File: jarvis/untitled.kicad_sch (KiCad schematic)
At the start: 17 parts, among them IC3 MCP73871T-4CAI_ML, IC4 TLV70033DDCT, J3 Conn_01x02 - Battery, U2 2137160001

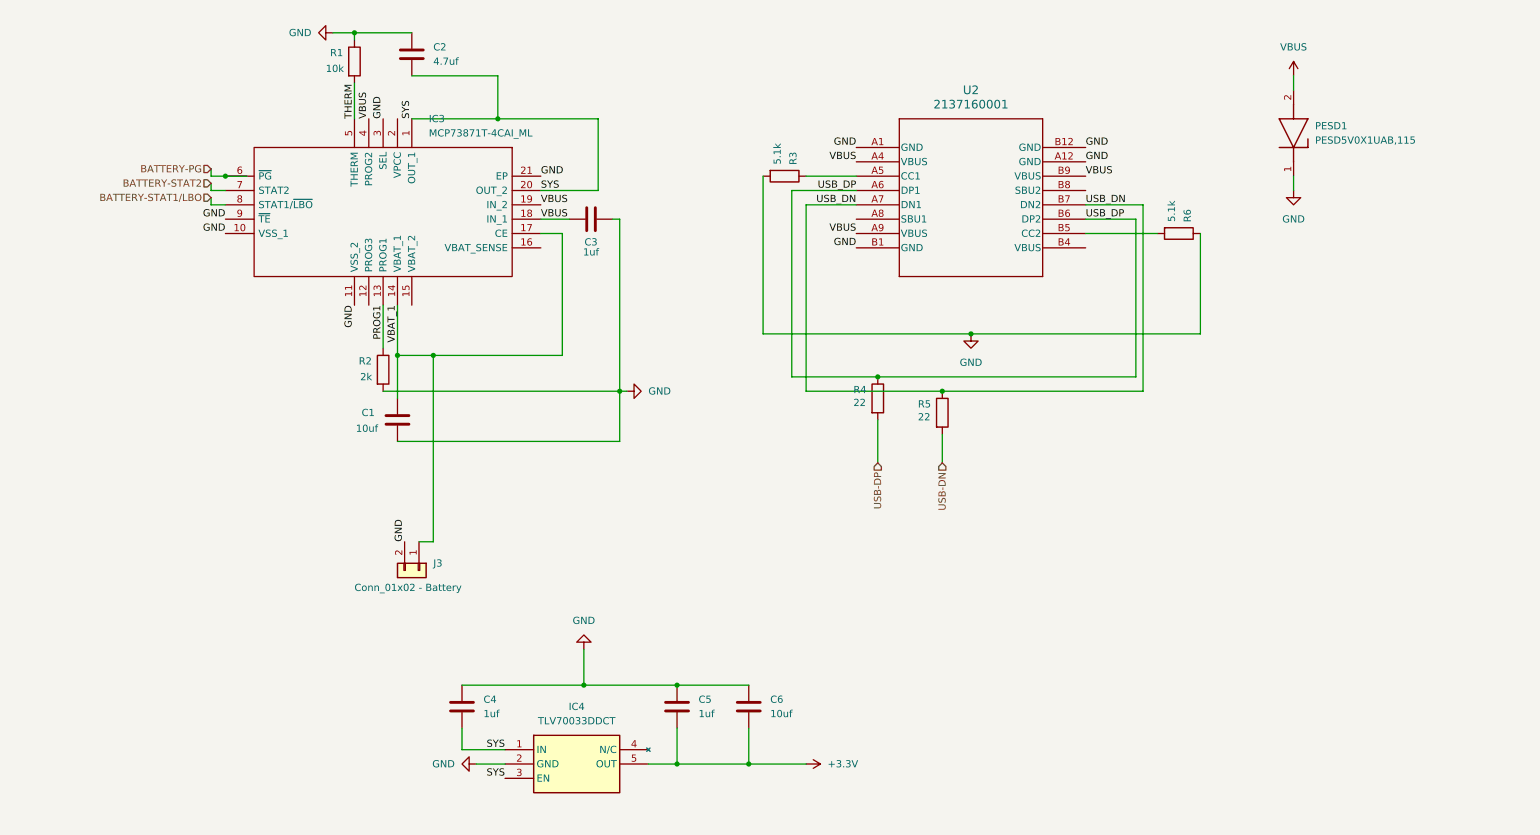
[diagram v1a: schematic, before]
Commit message: with leds and boot button
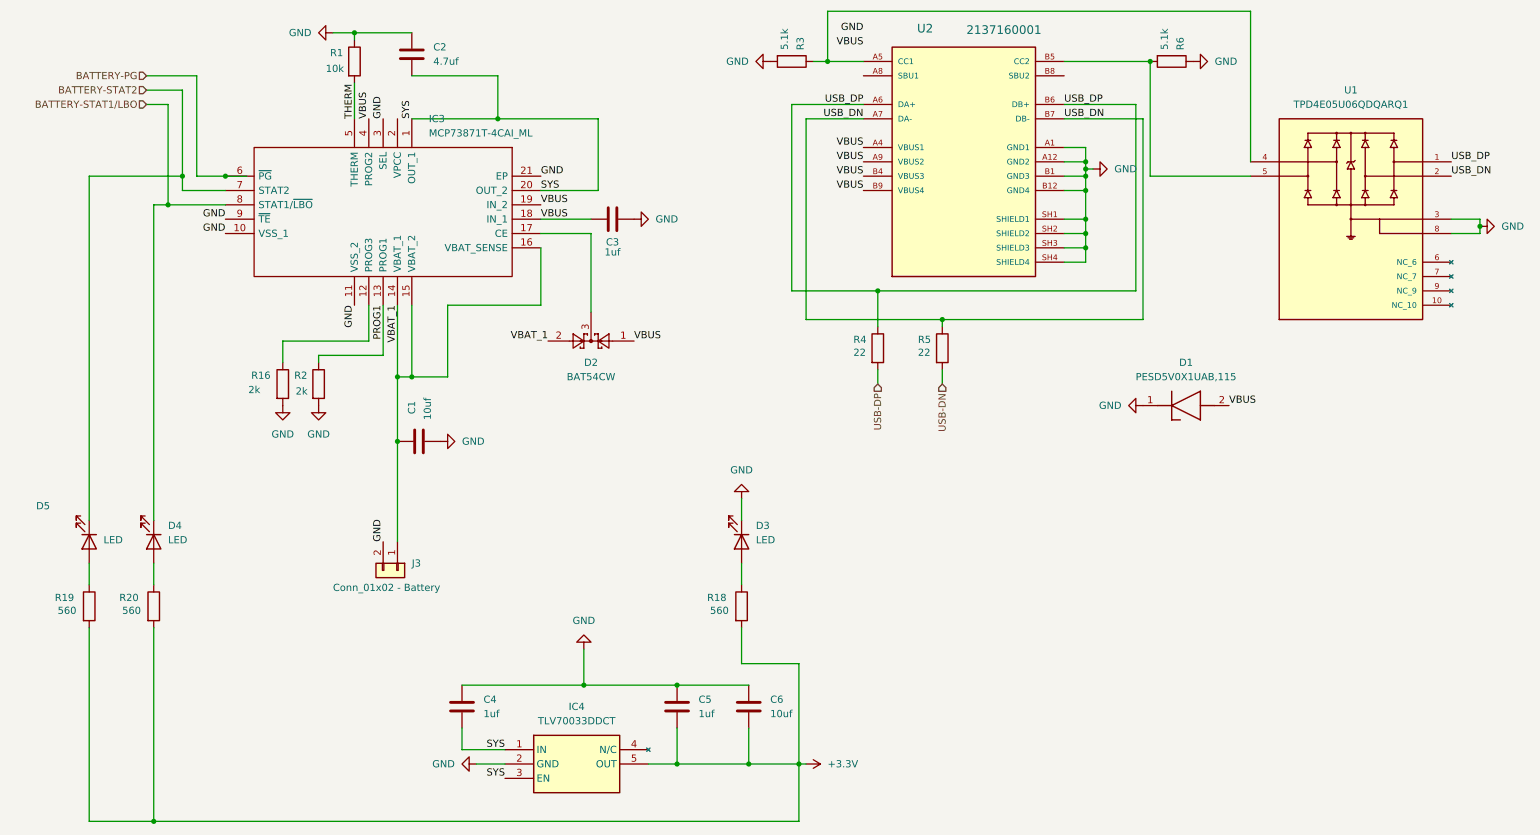
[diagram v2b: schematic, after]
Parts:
- removed PESD1: PESD5V0X1UAB,115, jarvis:PESD5V0X1UAB115, symbol jarvis:PESD5V0X1UAB,115
- added D1: PESD5V0X1UAB,115, jarvis:PESD5V0X1UAB115, symbol jarvis:PESD5V0X1UAB,115
- added D2: BAT54CW, Package_TO_SOT_SMD:SOT-323_SC-70_Handsoldering, symbol Diode:BAT54CW
- added D3, D4, D5: LED, LED_SMD:LED_0603_1608Metric, symbol Device:LED
- added R16: 2k, Resistor_SMD:R_0603_1608Metric, symbol Device:R
- added R18, R19, R20: 560, Resistor_SMD:R_0603_1608Metric, symbol Device:R
- added U1: TPD4E05U06QDQARQ1, jarvis:IC_TPD4E05U06QDQARQ1, symbol jarvis:TPD4E05U06QDQARQ1
- U2: footprint jarvis:2137160001_MOL -> jarvis:MOLEX_2137160001-holes; MANUFACTURER (none) -> Molex; MAXIMUM_PACKAGE_HEIGHT (none) -> 3.36mm; OPTION (none) -> MOLEX_CONFIG; PARTREV (none) -> B; STANDARD (none) -> Manufacturer Recommendations
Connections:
- net +3.3V: now also R18.2, R19.2, R20.2
- net BATTERY-STAT1/LBO: now also D4.1 (K)
- net BATTERY-STAT2: now also D5.1 (K)
- net GND: now also U2.SH1 (SHIELD1), U2.SH2 (SHIELD2), U2.SH3 (SHIELD3), U2.SH4 (SHIELD4), D1.1 (K), D3.1 (K), R16.2, U1.3, U1.8
- net USB_DN: now also U1.2
- net USB_DP: now also U1.1
- net VBAT_1: now also IC3.15 (VBAT_2), IC3.16 (VBAT_SENSE), D2.2; no longer IC3.17 (CE)
- net VBUS: now also U2.B4 (VBUS3), D1.2 (A), D2.1
- net at IC3.12 (PROG3): now also R16.1
- net at R3.1, U2.A5 (CC1): now also U1.4
- net at R6.2, U2.B5 (CC2): now also U1.5
- new net: D4.2 (A), R20.1
- new net: D2.3, IC3.17 (CE)
- new net: D3.2 (A), R18.1
- new net: D5.2 (A), R19.1
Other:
- moved on the sheet: C1, C3, J3, R2, R3, R4, R5, R6
